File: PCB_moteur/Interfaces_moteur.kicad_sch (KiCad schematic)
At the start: 25 parts, among them J3 Conn_01x02, J7 Conn_02x06_Top_Bottom, U12 MCP1802T-5002I/OT, U2 ISOW1044, U4 LSF0204PWR

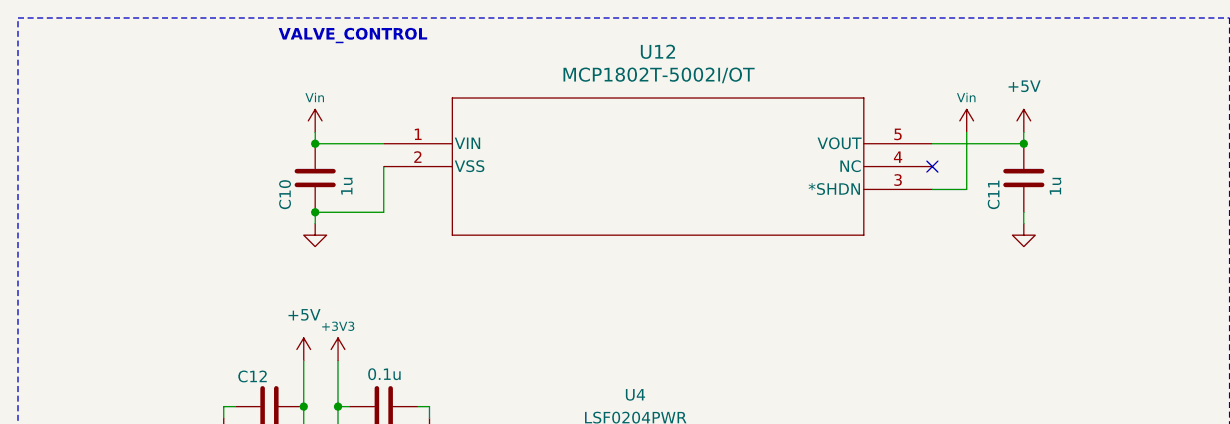
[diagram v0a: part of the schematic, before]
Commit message: fix: resistance ratios + typos
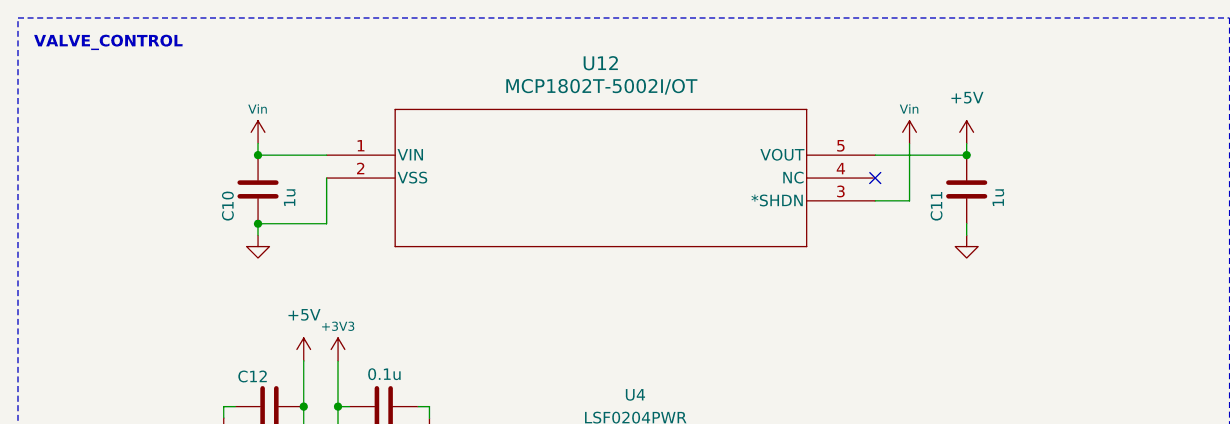
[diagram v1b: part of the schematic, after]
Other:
- moved on the sheet: C10, C11, U12
